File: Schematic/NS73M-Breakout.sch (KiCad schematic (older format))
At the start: 5 parts, among them P1 HEADER, P2 RF_OUT, U1 NS73M, Y1 32.768 KHz

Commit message: First revision of PCB including gerbers
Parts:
- C1: footprint (none) -> Capacitors_SMD:CP_Elec_4x4.5
- P1: footprint (none) -> NS73M-Breakout:Pin_Header_Angled_1x09_Pitch2.54mm_Reverse
- P2: footprint (none) -> Pin_Headers:Pin_Header_Angled_1x01_Pitch2.54mm
- U1: footprint (none) -> NS73M-Breakout:NS73M-DFN
- Y1: value 32.768 KHz -> 32.768 kHz; footprint (none) -> Crystals:Crystal_C26-LF_d2.1mm_l6.5mm_Horizontal_1EP_style1
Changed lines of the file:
@@
 F 0 "U1" H 5760 3050 60  0000 C CNN
 F 1 "NS73M" H 6160 3050 60  0000 C CNN
-F 2 "" H 6010 3140 60  0001 C CNN
+F 2 "NS73M-Breakout:NS73M-DFN" H 6010 3140 60  0001 C CNN
 F 3 "" H 6010 3140 60  0001 C CNN
 	1    6010 3790
@@
 P 6860 3470
 F 0 "Y1" V 6980 3590 50  0000 C CNN
-F 1 "32.768 KHz" V 7060 3770 50  0000 C CNN
-F 2 "" H 6860 3470 50  0000 C CNN
+F 1 "32.768 kHz" V 7060 3770 50  0000 C CNN
+F 2 "Crystals:Crystal_C26-LF_d2.1mm_l6.5mm_Horizontal_1EP_style1" H 6860 3470 50  0001 C CNN
 F 3 "" H 6860 3470 50  0000 C CNN
 	1    6860 3470
@@
 F 0 "C1" H 6130 4820 50  0000 L CNN
 F 1 "22uF" H 6280 4820 50  0000 L CNN
-F 2 "" H 6010 4820 50  0000 C CNN
+F 2 "Capacitors_SMD:CP_Elec_4x4.5" H 6010 4820 50  0001 C CNN
 F 3 "" H 6010 4820 50  0000 C CNN
 	1    6010 4820
@@
 F 0 "P1" H 4850 4190 50  0000 C CNN
 F 1 "HEADER" V 4950 3690 50  0001 C CNN
-F 2 "" H 4850 3690 50  0000 C CNN
+F 2 "NS73M-Breakout:Pin_Header_Angled_1x09_Pitch2.54mm_Reverse" H 4850 3690 50  0001 C CNN
 F 3 "" H 4850 3690 50  0000 C CNN
 	1    4850 3690
@@
 F 0 "P2" H 7120 4190 50  0000 C CNN
 F 1 "RF_OUT" H 7350 4290 50  0000 C CNN
-F 2 "" H 7130 4290 50  0000 C CNN
+F 2 "Pin_Headers:Pin_Header_Angled_1x01_Pitch2.54mm" H 7130 4290 50  0001 C CNN
 F 3 "" H 7130 4290 50  0000 C CNN
 	1    7130 4290
@@
 $Comp
 L PWR_FLAG #FLG02
-U 1 1 590943B8
-P 5390 4970
-F 0 "#FLG02" H 5390 5065 50  0001 C CNN
-F 1 "PWR_FLAG" H 5390 5150 50  0000 C CNN
-F 2 "" H 5390 4970 50  0000 C CNN
-F 3 "" H 5390 4970 50  0000 C CNN
-	1    5390 4970
-	-1   0    0    1
-$EndComp
-$Comp
-L PWR_FLAG #FLG03
 U 1 1 590943D2
 P 5660 4670
-F 0 "#FLG03" H 5660 4765 50  0001 C CNN
+F 0 "#FLG02" H 5660 4765 50  0001 C CNN
 F 1 "PWR_FLAG" H 5660 4850 50  0000 C CNN
 F 2 "" H 5660 4670 50  0000 C CNN
@@
 	5460 4670 6570 4670
 Connection ~ 5660 4670
+$Comp
+L PWR_FLAG #FLG03
+U 1 1 590943B8
+P 5390 4970
+F 0 "#FLG03" H 5390 5065 50  0001 C CNN
+F 1 "PWR_FLAG" H 5390 5150 50  0000 C CNN
+F 2 "" H 5390 4970 50  0000 C CNN
+F 3 "" H 5390 4970 50  0000 C CNN
+	1    5390 4970
+	-1   0    0    1
+$EndComp
 $EndSCHEMATC

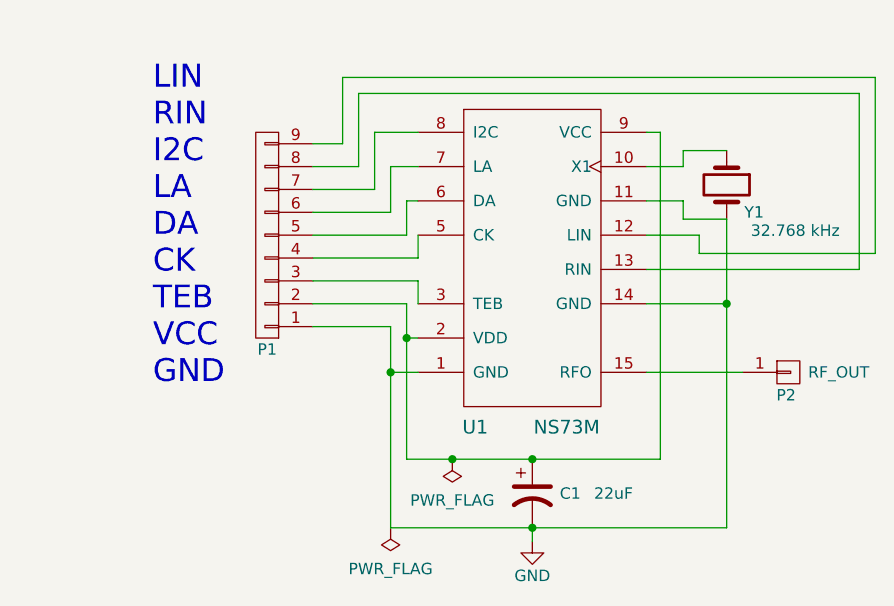
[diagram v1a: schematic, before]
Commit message: Cleaned up schematic, gerber packages, added license and PCB screencaps
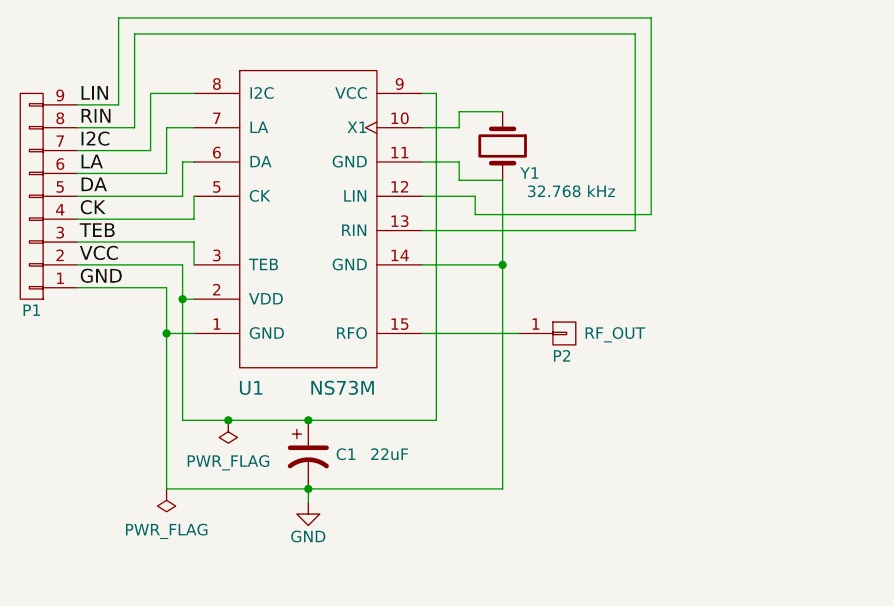
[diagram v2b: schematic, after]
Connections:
- net LIN: now reaches P1.9 (P9), U1.12 (LIN)
- net RIN: now reaches P1.8 (P8), U1.13 (RIN)
- net VCC: now reaches C1.1, P1.2 (P2), U1.2 (VDD), U1.9 (VCC)
- net TEB: now reaches P1.3 (P3), U1.3 (TEB)
- net CK: now reaches P1.4 (P4), U1.5 (CK)
- net DA: now reaches P1.5 (P5), U1.6 (DA)
- net LA: now reaches P1.6 (P6), U1.7 (LA)
- net I2C: now reaches P1.7 (P7), U1.8 (I2C)
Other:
- note removed: "LIN\nRIN\nI2C\nLA\nDA\nCK\nTEB\nVCC\nGND\n"
- moved on the sheet: C1, P1, P2, U1, Y1
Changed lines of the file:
@@
 Comp "Conor Peterson"
 Comment1 "conor.p.peterson@gmail.com"
-Comment2 ""
+Comment2 "CC-BY-4.0"
 Comment3 ""
 Comment4 ""
@@
 L NS73M U1
 U 1 1 590901B3
-P 6010 3790
-F 0 "U1" H 5760 3050 60  0000 C CNN
-F 1 "NS73M" H 6160 3050 60  0000 C CNN
-F 2 "NS73M-Breakout:NS73M-DFN" H 6010 3140 60  0001 C CNN
-F 3 "" H 6010 3140 60  0001 C CNN
-	1    6010 3790
+P 5030 3620
+F 0 "U1" H 4780 2880 60  0000 C CNN
+F 1 "NS73M" H 5180 2880 60  0000 C CNN
+F 2 "NS73M-Breakout:NS73M-DFN" H 5030 2970 60  0001 C CNN
+F 3 "" H 5030 2970 60  0001 C CNN
+	1    5030 3620
 	1    0    0    -1
 $EndComp
@@
 L Crystal Y1
 U 1 1 590901E6
-P 6860 3470
-F 0 "Y1" V 6980 3590 50  0000 C CNN
-F 1 "32.768 kHz" V 7060 3770 50  0000 C CNN
-F 2 "Crystals:Crystal_C26-LF_d2.1mm_l6.5mm_Horizontal_1EP_style1" H 6860 3470 50  0001 C CNN
-F 3 "" H 6860 3470 50  0000 C CNN
-	1    6860 3470
+P 5880 3300
+F 0 "Y1" V 6000 3420 50  0000 C CNN
+F 1 "32.768 kHz" V 6080 3600 50  0000 C CNN
+F 2 "Crystals:Crystal_C26-LF_d2.1mm_l6.5mm_Horizontal_1EP_style1" H 5880 3300 50  0001 C CNN
+F 3 "" H 5880 3300 50  0000 C CNN
+	1    5880 3300
 	0    1    1    0
 $EndComp
@@
 L CP1 C1
 U 1 1 59090277
-P 6010 4820
-F 0 "C1" H 6130 4820 50  0000 L CNN
-F 1 "22uF" H 6280 4820 50  0000 L CNN
-F 2 "Capacitors_SMD:CP_Elec_4x4.5" H 6010 4820 50  0001 C CNN
-F 3 "" H 6010 4820 50  0000 C CNN
-	1    6010 4820
-	1    0    0    -1
-$EndComp
-Text Notes 4350 4350 0    100  ~ 0
-LIN\nRIN\nI2C\nLA\nDA\nCK\nTEB\nVCC\nGND\n
-Wire Wire Line
-	5050 3490 5320 3490
-Wire Wire Line
-	5320 3490 5320 3240
-Wire Wire Line
-	5320 3240 5510 3240
-Wire Wire Line
-	5050 3590 5390 3590
-Wire Wire Line
-	5390 3590 5390 3390
-Wire Wire Line
-	5390 3390 5510 3390
-Wire Wire Line
-	5050 3690 5460 3690
-Wire Wire Line
-	5460 3690 5460 3540
-Wire Wire Line
-	5460 3540 5510 3540
-Wire Wire Line
-	5510 3690 5510 3690
-Wire Wire Line
-	5510 3690 5510 3790
-Wire Wire Line
-	5510 3790 5050 3790
+P 5030 4650
+F 0 "C1" H 5150 4650 50  0000 L CNN
+F 1 "22uF" H 5300 4650 50  0000 L CNN
+F 2 "Capacitors_SMD:CP_Elec_4x4.5" H 5030 4650 50  0001 C CNN
+F 3 "" H 5030 4650 50  0000 C CNN
+	1    5030 4650
+	1    0    0    -1
+$EndComp
 $Comp
 L CONN_01X09 P1
 U 1 1 590904E6
-P 4850 3690
-F 0 "P1" H 4850 4190 50  0000 C CNN
-F 1 "HEADER" V 4950 3690 50  0001 C CNN
-F 2 "NS73M-Breakout:Pin_Header_Angled_1x09_Pitch2.54mm_Reverse" H 4850 3690 50  0001 C CNN
-F 3 "" H 4850 3690 50  0000 C CNN
-	1    4850 3690
+P 3820 3520
+F 0 "P1" H 3820 4020 50  0000 C CNN
+F 1 "HEADER" V 3920 3520 50  0001 C CNN
+F 2 "NS73M-Breakout:Pin_Header_Angled_1x09_Pitch2.54mm_Reverse" H 3820 3520 50  0001 C CNN
+F 3 "" H 3820 3520 50  0000 C CNN
+	1    3820 3520
 	-1   0    0    1
 $EndComp
-Wire Wire Line
-	5050 3890 5510 3890
-Wire Wire Line
-	5510 3890 5510 3990
-Wire Wire Line
-	5050 3990 5460 3990
-Wire Wire Line
-	5460 3990 5460 4670
-Wire Wire Line
-	5460 4140 5510 4140
-Wire Wire Line
-	5050 4090 5390 4090
-Wire Wire Line
-	5390 4090 5390 4970
-Wire Wire Line
-	5390 4290 5510 4290
 $Comp
 L GND #PWR01
 U 1 1 59090A59
-P 6010 5030
-F 0 "#PWR01" H 6010 4780 50  0001 C CNN
-F 1 "GND" H 6010 4880 50  0000 C CNN
-F 2 "" H 6010 5030 50  0000 C CNN
-F 3 "" H 6010 5030 50  0000 C CNN
-	1    6010 5030
-	1    0    0    -1
-$EndComp
-Wire Wire Line
-	6570 4670 6570 3240
-Wire Wire Line
-	6570 3240 6510 3240
-Connection ~ 5460 4140
-Connection ~ 5390 4290
+P 5030 4860
+F 0 "#PWR01" H 5030 4610 50  0001 C CNN
+F 1 "GND" H 5030 4710 50  0000 C CNN
+F 2 "" H 5030 4860 50  0000 C CNN
+F 3 "" H 5030 4860 50  0000 C CNN
+	1    5030 4860
+	1    0    0    -1
+$EndComp
 $Comp
 L CONN_01X01 P2
 U 1 1 59090C31
-P 7130 4290
-F 0 "P2" H 7120 4190 50  0000 C CNN
-F 1 "RF_OUT" H 7350 4290 50  0000 C CNN
-F 2 "Pin_Headers:Pin_Header_Angled_1x01_Pitch2.54mm" H 7130 4290 50  0001 C CNN
-F 3 "" H 7130 4290 50  0000 C CNN
-	1    7130 4290
-	1    0    0    -1
-$EndComp
-Wire Wire Line
-	6510 4290 6930 4290
-Wire Wire Line
-	6510 3390 6670 3390
-Wire Wire Line
-	6670 3390 6670 3320
-Wire Wire Line
-	6670 3320 6860 3320
-Wire Wire Line
-	6510 3540 6670 3540
-Wire Wire Line
-	6670 3540 6670 3620
-Wire Wire Line
-	6670 3620 6860 3620
-Wire Wire Line
-	6510 3990 6860 3990
-Wire Wire Line
-	6860 3620 6860 4970
-Connection ~ 6860 3990
-Wire Wire Line
-	6860 4970 5390 4970
-Connection ~ 6010 4670
-Wire Wire Line
-	5050 3390 5250 3390
-Wire Wire Line
-	5250 3390 5250 3070
-Wire Wire Line
-	5250 3070 7440 3070
-Wire Wire Line
-	7440 3070 7440 3840
-Wire Wire Line
-	7440 3840 6510 3840
-Wire Wire Line
-	5050 3290 5180 3290
-Wire Wire Line
-	5180 3290 5180 3000
-Wire Wire Line
-	5180 3000 7510 3000
-Wire Wire Line
-	7510 3000 7510 3770
-Wire Wire Line
-	7510 3770 6740 3770
-Wire Wire Line
-	6740 3770 6740 3690
-Wire Wire Line
-	6740 3690 6510 3690
-Wire Wire Line
-	6010 5030 6010 4970
-Connection ~ 6010 4970
+P 6150 4120
+F 0 "P2" H 6140 4020 50  0000 C CNN
+F 1 "RF_OUT" H 6370 4120 50  0000 C CNN
+F 2 "Pin_Headers:Pin_Header_Angled_1x01_Pitch2.54mm" H 6150 4120 50  0001 C CNN
+F 3 "" H 6150 4120 50  0000 C CNN
+	1    6150 4120
+	1    0    0    -1
+$EndComp
 $Comp
 L PWR_FLAG #FLG02
 U 1 1 590943D2
-P 5660 4670
-F 0 "#FLG02" H 5660 4765 50  0001 C CNN
-F 1 "PWR_FLAG" H 5660 4850 50  0000 C CNN
-F 2 "" H 5660 4670 50  0000 C CNN
-F 3 "" H 5660 4670 50  0000 C CNN
-	1    5660 4670
+P 4680 4500
+F 0 "#FLG02" H 4680 4595 50  0001 C CNN
+F 1 "PWR_FLAG" H 4680 4680 50  0000 C CNN
+F 2 "" H 4680 4500 50  0000 C CNN
+F 3 "" H 4680 4500 50  0000 C CNN
+	1    4680 4500
 	-1   0    0    1
 $EndComp
-Wire Wire Line
-	5460 4670 6570 4670
-Connection ~ 5660 4670
 $Comp
 L PWR_FLAG #FLG03
 U 1 1 590943B8
-P 5390 4970
-F 0 "#FLG03" H 5390 5065 50  0001 C CNN
-F 1 "PWR_FLAG" H 5390 5150 50  0000 C CNN
-F 2 "" H 5390 4970 50  0000 C CNN
-F 3 "" H 5390 4970 50  0000 C CNN
-	1    5390 4970
+P 4410 4800
+F 0 "#FLG03" H 4410 4895 50  0001 C CNN
+F 1 "PWR_FLAG" H 4410 4980 50  0000 C CNN
+F 2 "" H 4410 4800 50  0000 C CNN
+F 3 "" H 4410 4800 50  0000 C CNN
+	1    4410 4800
 	-1   0    0    1
 $EndComp
+Text Label 4030 3920 0    60   ~ 0
+GND
+Text Label 4030 3820 0    60   ~ 0
+VCC
+Text Label 4030 3720 0    60   ~ 0
+TEB
+Text Label 4030 3620 0    60   ~ 0
+CK
+Text Label 4030 3520 0    60   ~ 0
+DA
+Text Label 4030 3420 0    60   ~ 0
+LA
+Text Label 4030 3320 0    60   ~ 0
+I2C
+Text Label 4030 3220 0    60   ~ 0
+RIN
+Text Label 4030 3120 0    60   ~ 0
+LIN
+Wire Wire Line
+	4340 3320 4340 3070
+Wire Wire Line
+	4340 3070 4530 3070
+Wire Wire Line
+	4410 3420 4410 3220
+Wire Wire Line
+	4410 3220 4530 3220
+Wire Wire Line
+	4480 3520 4480 3370
+Wire Wire Line
+	4480 3370 4530 3370
+Wire Wire Line
+	4530 3520 4530 3520
+Wire Wire Line
+	4530 3520 4530 3620
+Wire Wire Line
+	4530 3720 4530 3820
+Wire Wire Line
+	4480 3820 4480 4500
+Wire Wire Line
+	4480 3970 4530 3970
+Wire Wire Line
+	4410 3920 4410 4800
+Wire Wire Line
+	4410 4120 4530 4120
+Wire Wire Line
+	5590 4500 5590 3070
+Wire Wire Line
+	5590 3070 5530 3070
+Connection ~ 4480 3970
+Connection ~ 4410 4120
+Wire Wire Line
+	5530 4120 5950 4120
+Wire Wire Line
+	5530 3220 5690 3220
+Wire Wire Line
+	5690 3220 5690 3150
+Wire Wire Line
+	5690 3150 5880 3150
+Wire Wire Line
+	5530 3370 5690 3370
+Wire Wire Line
+	5690 3370 5690 3450
+Wire Wire Line
+	5690 3450 5880 3450
+Wire Wire Line
+	5530 3820 5880 3820
+Wire Wire Line
+	5880 4800 5880 3450
+Connection ~ 5880 3820
+Wire Wire Line
+	4410 4800 5880 4800
+Connection ~ 5030 4500
+Wire Wire Line
+	4270 3220 4270 2810
+Wire Wire Line
+	4270 2810 6460 2810
+Wire Wire Line
+	6460 2810 6460 3670
+Wire Wire Line
+	6460 3670 5530 3670
+Wire Wire Line
+	4200 3120 4200 2740
+Wire Wire Line
+	4200 2740 6530 2740
+Wire Wire Line
+	6530 2740 6530 3600
+Wire Wire Line
+	6530 3600 5760 3600
+Wire Wire Line
+	5760 3600 5760 3520
+Wire Wire Line
+	5760 3520 5530 3520
+Wire Wire Line
+	5030 4860 5030 4800
+Connection ~ 5030 4800
+Wire Wire Line
+	4480 4500 5590 4500
+Connection ~ 4680 4500
+Wire Wire Line
+	4200 3120 4020 3120
+Wire Wire Line
+	4270 3220 4020 3220
+Wire Wire Line
+	4020 3320 4340 3320
+Wire Wire Line
+	4020 3420 4410 3420
+Wire Wire Line
+	4020 3520 4480 3520
+Wire Wire Line
+	4530 3620 4020 3620
+Wire Wire Line
+	4020 3720 4530 3720
+Wire Wire Line
+	4020 3820 4480 3820
+Wire Wire Line
+	4020 3920 4410 3920
 $EndSCHEMATC
